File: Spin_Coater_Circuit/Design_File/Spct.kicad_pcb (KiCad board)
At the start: 2 copper layers, 88 x 120 mm, 67 parts, among them J1 EH_B2B-EH-A, J2 EH_B3B-EH-A, J3 EH_B8B-EH-A, J4 EH_B2B-EH-A, J5 EH_B4B-EH-A, J6 EH_B2B-EH-A, J7 EH_B6B-EH-A, J8 EH_B2B-EH-A, J9 EH_B2B-EH-A, Q1 2N7002, Q2 2N7002, Q3 2N7002, U1 NUCLEO-F411RE, U2 MCP4922-E/SL, U3 367661, U4 24LC512T-I/SN, U6 ISL85410FRZ

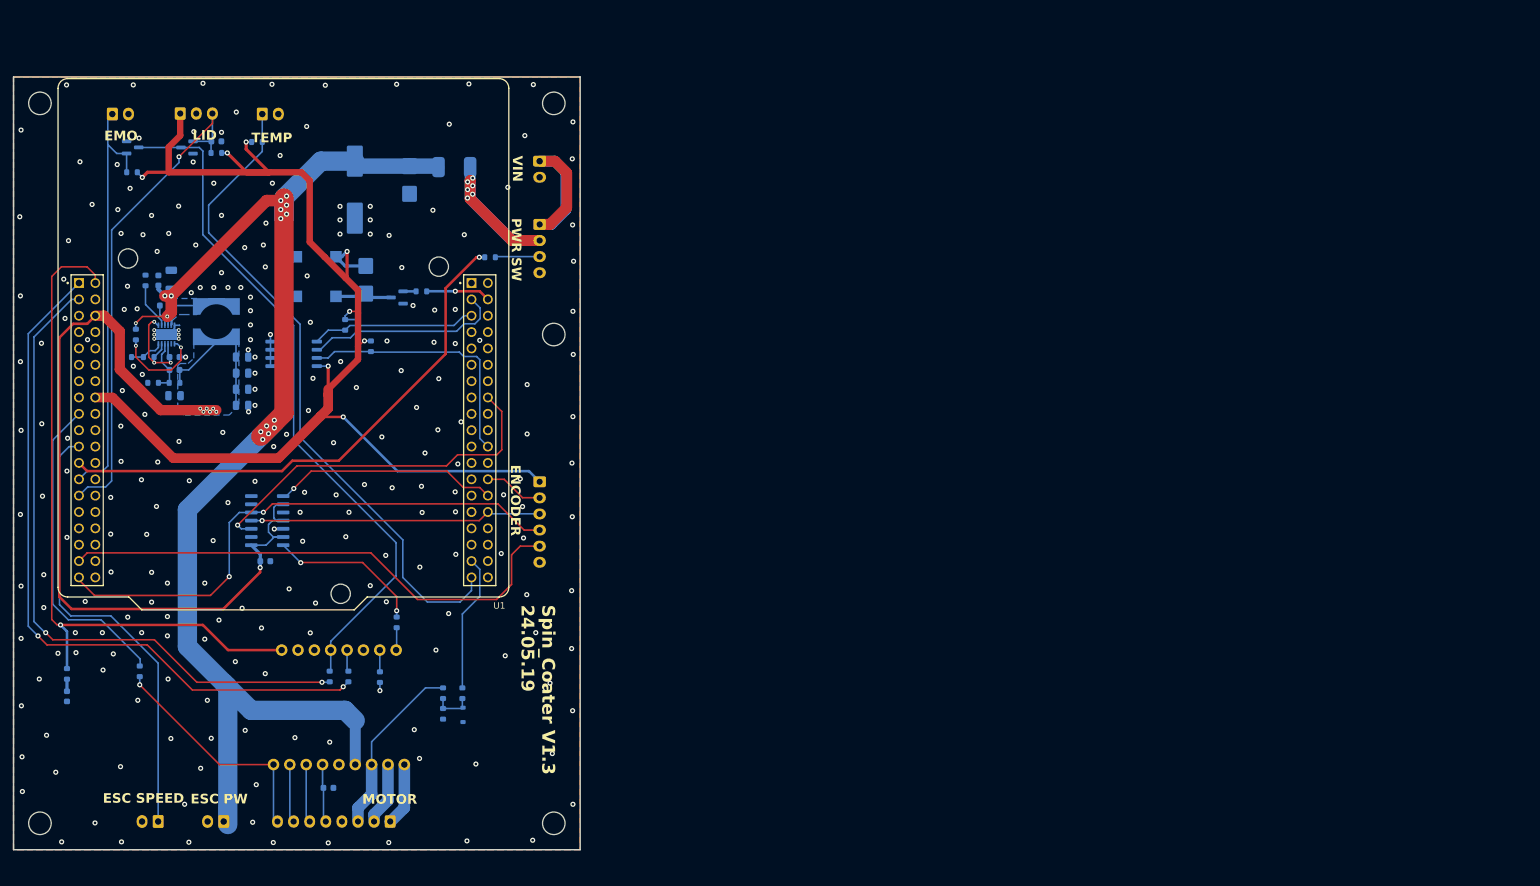
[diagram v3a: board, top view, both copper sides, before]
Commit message: Place Arduino pinout / Drv socket
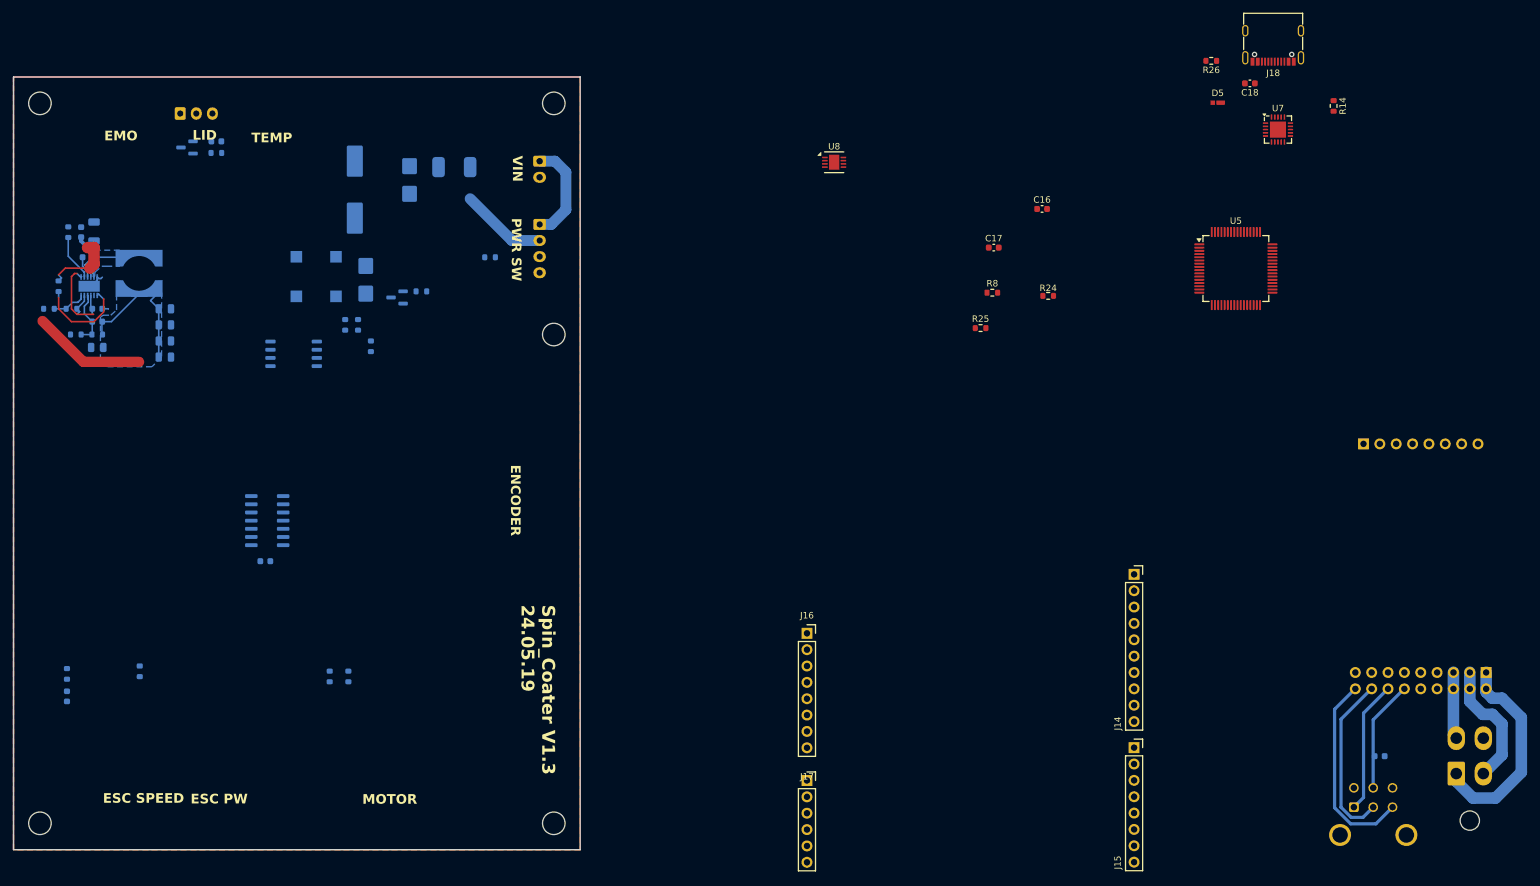
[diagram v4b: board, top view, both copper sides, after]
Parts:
- removed D3: MM3Z3V3T1G, Custom_Library:D_SOD-323-2
- removed J3: EH_B8B-EH-A, Connector_JST:JST_EH_B8B-EH-A_1x08_P2.50mm_Vertical
- removed J4, J6, J8, J9: EH_B2B-EH-A, Connector_JST:JST_EH_B2B-EH-A_1x02_P2.50mm_Vertical
- removed J7: EH_B6B-EH-A, Connector_JST:JST_EH_B6B-EH-A_1x06_P2.50mm_Vertical
- removed Q2: 2N7002, Package_TO_SOT_SMD:SOT-23
- removed R10: 4.7k, Resistor_SMD:R_0603_1608Metric
- removed R2: 75k, Resistor_SMD:R_0603_1608Metric
- removed R3: 10k, Resistor_SMD:R_0603_1608Metric
- removed R4, R9: 100, Resistor_SMD:R_0603_1608Metric
- removed U1: NUCLEO-F411RE, Module:ST_NUCLEO-F401RE
- removed U3: 367661, Connector_Pin:MAXON_DRV
- added C16: 100nF/50V, Capacitor_SMD:C_0603_1608Metric, F.Cu at (198.8, 52.9)
- added C17: 2.2uF/10V, Capacitor_SMD:C_0603_1608Metric, F.Cu at (191.3, 58.9)
- added C18: 100nF/50V, Capacitor_SMD:C_0603_1608Metric, F.Cu at (231.1, 33.4)
- added D5: NSR20F30NXT5G, Custom_Library:DSN2-152AB_ONS, F.Cu at (226.1, 36.4)
- added J10: Conn_01x08, Connector_PinSocket_2.54mm:PinSocket_1x08_P2.54mm_Vertical, B.Cu at (248.7, 89.4)
- added J11: Conn_02x09_Odd_Even, Connector_PinSocket_2.54mm:PinSocket_2x09_P2.54mm_Vertical, B.Cu at (267.8, 124.9)
- added J12: Motor_Output, Connector_Molex:Molex_Mini-Fit_Jr_5569-04A2_2x02_P4.20mm_Horizontal, B.Cu at (263.1, 140.6)
- added J13: Motor_Feedback, Connector_Molex:Molex_Micro-Fit_3.0_43045-0621_2x03-1MP_P3.00mm_Horizontal, B.Cu at (247.2, 145.8)
- added J14: Conn_01x10, Connector_PinSocket_2.54mm:PinSocket_1x10_P2.54mm_Vertical, F.Cu at (213.1, 109.6)
- added J15: Conn_01x08, Connector_PinSocket_2.54mm:PinSocket_1x08_P2.54mm_Vertical, F.Cu at (213.1, 136.5)
- added J16: Conn_01x08, Connector_PinSocket_2.54mm:PinSocket_1x08_P2.54mm_Vertical, F.Cu at (162.3, 118.8)
- added J17: Conn_01x06, Connector_PinSocket_2.54mm:PinSocket_1x06_P2.54mm_Vertical, F.Cu at (162.3, 141.6)
- added J18: USB_C_Receptacle_USB2.0_14P, Connector_USB:USB_C_Receptacle_G-Switch_GT-USB-7010ASV, F.Cu at (234.7, 26.3)
- added R24: 100, Resistor_SMD:R_0603_1608Metric, F.Cu at (199.7, 66.4)
- added R25: 100k, Resistor_SMD:R_0603_1608Metric, F.Cu at (189.2, 71.4)
- added R26: 5.1k, Resistor_SMD:R_0603_1608Metric, F.Cu at (225.1, 29.9)
- added U5: STM32F411RETx, Package_QFP:LQFP-64_10x10mm_P0.5mm, F.Cu at (228.9, 62.1)
- added U7: FT231XQ, Package_DFN_QFN:QFN-20-1EP_4x4mm_P0.5mm_EP2.5x2.5mm, F.Cu at (235.4, 40.6)
- added U8: ADPL42005ACPZ-3.3-R7, Package_CSP:LFCSP-8-1EP_3x3mm_P0.5mm_EP1.6x2.34mm, F.Cu at (166.5, 45.6)
- R14: value 10k -> 5.1k; moved to F.Cu
- R8: moved to F.Cu
- moved R14 186.9 mm to (244.1, 36.9), turned to -90 degrees
- moved C2 163.3 mm to (251.2, 137.9)
- moved R8 116.6 mm to (191.1, 65.9)
- moved L1 14.2 mm to (58.6, 62.9)
- moved C10 14.2 mm to (52.1, 74.4)
- moved C11 14.2 mm to (62.6, 75.9)
- moved C12 14.2 mm to (52.1, 76.4)
- moved C13 14.2 mm to (62.6, 73.4)
- moved C14 14.2 mm to (62.6, 70.9)
- moved C15 14.2 mm to (62.6, 68.4)
- moved C8 14.2 mm to (52.1, 68.4)
- moved C9 14.2 mm to (52.1, 70.4)
- moved R19 14.2 mm to (52.1, 72.4)
- moved C7 14.2 mm to (50.6, 60.4)
- moved C5 14.2 mm to (51.6, 56.4)
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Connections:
- C2 pad 1: Net-(J3-Pin_5) -> /5V_HALL
- R11 pad 2: Net-(J3-Pin_8) -> /HALL_3
- R14 pad 1: +3V3 -> Net-(J18-CC1)
- R14 pad 2: EMO -> GND
- R8 pad 1: +3V3 -> GND
- R8 pad 2: TEMP -> Net-(U5-BOOT0)
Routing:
- net +3V3: track 200.6 -> 0.00 mm, vias 8 -> 0
- net +24V: track 212.6 -> 15.6 mm, vias 16 -> 0
- net +E5V: track 150.9 -> 38.2 mm, vias 7 -> 0
- net DIR: track 110.9 -> 0.00 mm, vias 2 -> 0
- net Net-(J10-Pin_4): track 107.7 -> 0.00 mm
- net READY_IN: track 107.3 -> 0.00 mm, vias 1 -> 0
- net DRV_EN: track 103.5 -> 0.00 mm, vias 2 -> 0
- net TEMP: track 102.9 -> 0.00 mm
- net MOSI: track 85.7 -> 0.00 mm, vias 2 -> 0
- net SW_LED: track 83.3 -> 0.00 mm, vias 1 -> 0
- net MISO: track 81.2 -> 0.00 mm
- net Lid_Sensor: track 78.1 -> 0.00 mm, vias 1 -> 0
- net PWM_SPEED: track 70.7 -> 0.00 mm
- net EMO: track 66.7 -> 0.00 mm
- net ADC_CS: track 57.3 -> 0.00 mm, vias 1 -> 0
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
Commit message: finalize layout
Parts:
- added C19: 10uF/10V, Capacitor_SMD:C_0805_2012Metric, F.Cu at (103.2, 53.4)
- added C20: 100nF/50V, Capacitor_SMD:C_0603_1608Metric, F.Cu at (101.4, 53.6)
- added D3: 150060BS55040, LED_SMD:LED_0603_1608Metric, F.Cu at (119.9, 86.0)
- added D6: 150060BS55040, LED_SMD:LED_0603_1608Metric, F.Cu at (119.9, 89.4)
- added D8: MMSZ5245, Diode_SMD:D_SOD-123, F.Cu at (53.8, 56.4)
- added J3: FTSH-105-01-L-DV-K-TR, Custom_Library:PinHeader_2x05_P1.27mm_Vertical_SMD, B.Cu at (119.4, 57.6)
- added Q4: Si7461DP, Package_SO:PowerPAK_SO-8_Single, F.Cu at (60.8, 56.0)
- added R10: 470k, Resistor_SMD:R_0603_1608Metric, F.Cu at (48.2, 72.5)
- added R2: 1k, Resistor_SMD:R_0603_1608Metric, F.Cu at (123.1, 86.0)
- added R3: 1k, Resistor_SMD:R_0603_1608Metric, F.Cu at (123.1, 89.4)
- added R4: 330k, Resistor_SMD:R_0603_1608Metric, F.Cu at (55.9, 57.3)
- added R9: 10, Resistor_SMD:R_0603_1608Metric, F.Cu at (56.6, 59.8)
- C1, C10, C11, C12, C13, C14, C15, C2, C3, C4, C5, C6, C7, C8, C9, D1, D2, D4, L1, LS1, Q1, Q3, R1, R11, R12, R13, R15, R16, R17, R18, R19, R20, R21, R22, R23, R5, R6, R7, U2, U6: moved to F.Cu
- F1: value 0679H5000-01 -> 0679H7000-01; moved to F.Cu
- J1: value EH_B2B-EH-A -> Mini-Fit(5569-02A); footprint Connector_JST:JST_EH_B2B-EH-A_1x02_P2.50mm_Vertical -> Connector_Molex:Molex_Mini-Fit_Jr_5569-02A2_2x01_P4.20mm_Horizontal
- U4: footprint Package_SO:SOIC-8_5.275x5.275mm_P1.27mm -> Package_SO:SOIC-8_5.3x5.3mm_P1.27mm; moved to F.Cu
- moved J12 208.5 mm to (54.6, 135.6), turned to -90 degrees
- moved J13 199.5 mm to (49.4, 119.7), turned to -90 degrees
- moved J11 198.0 mm to (70.3, 140.3), turned to 0 degrees
- moved C2 196.8 mm to (55.0, 123.6), turned to -90 degrees
- moved U5 148.7 mm to (82.1, 85.7), turned to 180 degrees
- moved J10 146.4 mm to (105.8, 121.2), turned to 180 degrees
- moved C18 129.8 mm to (101.9, 46.1)
- moved R14 129.5 mm to (114.6, 40.1)
- moved U7 128.6 mm to (107.0, 46.7), turned to 180 degrees
- moved J18 128.0 mm to (107.0, 35.2)
- moved R26 125.8 mm to (99.6, 40.1), turned to -90 degrees
- moved D5 125.8 mm to (100.4, 42.9)
- moved R24 124.0 mm to (99.4, 139.2), turned to 180 degrees
- moved C16 123.8 mm to (77.3, 76.8), turned to 90 degrees
- moved C17 113.5 mm to (79.2, 76.8), turned to 90 degrees
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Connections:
- net /USB_DM renamed /USB_D-
- net /USB_DP renamed /USB_D+
- C10 pad 1: +E5V -> +5V
- C11 pad 1: +E5V -> +5V
- C12 pad 1: +E5V -> +5V
- C13 pad 1: +E5V -> +5V
- C14 pad 1: +E5V -> +5V
- C15 pad 1: +E5V -> +5V
- C3 pad 1: +E5V -> +5V
- C9 pad 1: +E5V -> +5V
- D5 pad 1: +E5V -> +5V
- F1 pad 1: +24V -> Net-(D8-K)
- F1 pad 2: Net-(J5-Pin_2) -> Net-(J1-Pin_1)
- J11 pad 11: /5V_HALL -> unconnected-(J11-Pin_11-Pad11)
- J11 pad 12: unconnected-(J11-Pin_12-Pad12) -> /5V_HALL
- J11 pad 13: /HALL_1 -> GND
- J11 pad 14: GND -> /HALL_1
- J11 pad 15: /HALL_2 -> GND
- J11 pad 16: GND -> /HALL_2
- J11 pad 17: /HALL_3 -> GND
- J11 pad 18: GND -> /HALL_3
- J14 pad 5: /SD_CLK -> SPI1_CLK_SD
- J14 pad 6: /SD_MISO -> SPI1_MISO_SD
- J14 pad 7: /SD_MOSI -> SPI1_MOSI_SD
- J14 pad 8: /SD_CS -> SPI1_CS_SD
- J5 pad 1: Net-(J1-Pin_1) -> Net-(D8-A)
- L1 pad 2: +E5V -> +5V
- R11 pad 1: cRPM_METER -> RPM_METER_IC
- R12 pad 2: pBuzzer -> Buzzer_PWM
- R16 pad 2: SDA -> I2C1_SDA
- R17 pad 2: SCL -> I2C1_SCL
- R18 pad 2: WP -> EEPROM_WP
- R19 pad 1: +E5V -> +5V
- U2 pad 1: +E5V -> +5V
- U2 pad 11: +E5V -> +5V
- U2 pad 13: +E5V -> +5V
- U2 pad 3: ADC_CS -> SPI2_ADC_CS
- U2 pad 4: SCK -> SPI2_ADC_CLK
- U2 pad 5: MOSI -> SPI2_ADC_MOSI
- U2 pad 9: +E5V -> +5V
- U4 pad 5: SDA -> I2C1_SDA
- U4 pad 6: SCL -> I2C1_SCL
- U4 pad 7: WP -> EEPROM_WP
- U5 pad 1: unconnected-(U5-VBAT-Pad1) -> +3V3
- U5 pad 11: SPI2_MOSI -> SPI2_ADC_MOSI
- U5 pad 28: EEPROM_WP -> unconnected-(U5-PB2-Pad28)
- U5 pad 34: SPI2_CLK -> SPI2_ADC_CLK
- U5 pad 36: unconnected-(U5-PB15-Pad36) -> /LCD_RD_DI
- U5 pad 38: unconnected-(U5-PC7-Pad38) -> /LCD_WR_DO
- U5 pad 41: unconnected-(U5-PA8-Pad41) -> /LCD_RS_DO
- U5 pad 44: unconnected-(U5-PA11-Pad44) -> /LCD_CS_DO
- U5 pad 45: unconnected-(U5-PA12-Pad45) -> /LCD_RST_DO
- U5 pad 58: unconnected-(U5-PB6-Pad58) -> EEPROM_WP
- U8 pad 5: +E5V -> +5V
- U8 pad 8: +E5V -> +5V
- U8 pad 9: (no net) -> GND
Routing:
- net +3V3: track 0.00 -> 248.4 mm, vias 0 -> 11
- net +5V: track 0.00 -> 223.3 mm, vias 0 -> 10
- net +24V: track 15.6 -> 142.8 mm, vias 0 -> 12
- net Net-(J10-Pin_4): track 0.00 -> 114.6 mm, vias 0 -> 2
- net /MCU_RST: track 0.00 -> 98.8 mm, vias 0 -> 3
- net READY_IN: track 0.00 -> 97.5 mm, vias 0 -> 2
- net /DEBUG_SWCLK: track 0.00 -> 65.9 mm, vias 0 -> 3
- net UART1_TX: track 0.00 -> 65.8 mm, vias 0 -> 2
- net UART1_RX: track 0.00 -> 65.4 mm, vias 0 -> 2
- net /DEBUG_SWDIO: track 0.00 -> 65.2 mm, vias 0 -> 3
- net Lid_Sensor: track 0.00 -> 64.9 mm, vias 0 -> 2
- net /DEBUG_SWO: track 0.00 -> 64.2 mm, vias 0 -> 3
- net DRV_EN: track 0.00 -> 62.1 mm, vias 0 -> 2
- net DIR: track 0.00 -> 61.9 mm, vias 0 -> 2
- net SW_LED: track 0.00 -> 56.3 mm
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- added copper zone on F.Cu, net +24V
- added copper zone on F.Cu, net +3V3
- added copper zone on F.Cu, net +5V
- added copper zone on F.Cu, net Net-(D8-K)
- added copper zone on F.Cu, net Net-(J1-Pin_1)
- added copper zone on F.Cu, net Net-(U6-PHASE)
- removed copper zone on B.Cu, net +E5V
- removed copper zone on B.Cu, net Net-(U6-PHASE)
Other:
- board text added: "3.3V"
- board text added: "5V"
- board text added: "DRV_RDY"
- board text added: "Spin_Coater V2.0 25.08.17"
- board text removed: "EMO"
- board text removed: "ENCODER"
- board text removed: "ESC PW"
- board text removed: "ESC SPEED"
- board text removed: "MOTOR"
- board text removed: "Spin_Coater V1.3 24.05.19"
- board text removed: "TEMP"

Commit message: Output setup & layout minor fix
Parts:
- added R27: 100k, Resistor_SMD:R_0603_1608Metric, F.Cu at (84.6, 41.4)
- J1: footprint Connector_Molex:Molex_Mini-Fit_Jr_5569-02A2_2x01_P4.20mm_Horizontal -> Custom_Library:Molex_Mini-Fit_Jr_5569-02A2_2x01_P4.20mm_Horizontal
- J12: footprint Connector_Molex:Molex_Mini-Fit_Jr_5569-04A2_2x02_P4.20mm_Horizontal -> Custom_Library:Molex_Mini-Fit_Jr_5569-04A2_2x02_P4.20mm_Horizontal
- J13: footprint Connector_Molex:Molex_Micro-Fit_3.0_43045-0621_2x03-1MP_P3.00mm_Horizontal -> Custom_Library:Molex_Micro-Fit_3.0_43045-0621_2x03-1MP_P3.00mm_Horizontal
- Q4: value Si7461DP -> SI7461DP-T1-GE3; footprint Package_SO:PowerPAK_SO-8_Single -> Custom_Library:PowerPAK_SO-8_Single
- moved J15 2.49 mm to (107.1, 93.7)
- moved J14 2.49 mm to (107.1, 66.8)
- moved Q3 1.07 mm to (84.6, 44.5)
- moved REF** 0.14 mm to (43.1, 148.4)
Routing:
- net GND: track 36.4 -> 44.2 mm, vias 233 -> 343
- net /LCD_D5_DO: track 25.8 -> 23.0 mm
- net SPI1_MOSI_SD: track 29.0 -> 26.4 mm
- net /LCD_D6_DO: track 24.9 -> 22.4 mm
- net /LCD_D4_DO: track 34.5 -> 32.0 mm
- net /LCD_D3_DO: track 36.4 -> 33.9 mm
- net /LCD_D2_DO: track 38.3 -> 35.7 mm
- net /LCD_D7_DO: track 24.1 -> 21.5 mm
- net /LCD_D0_DO: track 36.0 -> 33.4 mm
- net SPI1_CS_SD: track 22.2 -> 19.6 mm
- net SPI1_CLK_SD: track 28.0 -> 25.4 mm
- net SPI1_MISO_SD: track 28.6 -> 26.0 mm
- net /LCD_D1_DO: track 34.3 -> 31.8 mm
- net /DEBUG_SWO: track 64.2 -> 65.8 mm
- net /MCU_RST: track 98.8 -> 100.3 mm
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- added copper zone on B.Cu, net (none)
- added copper zone on F.Cu, net (none)
